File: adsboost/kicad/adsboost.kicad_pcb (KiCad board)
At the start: 4 copper layers, 35.7 x 18 mm, 19 parts, among them J1 ANT_IN, J2 RF_OUT+BIAS, U1 TQP3M9036

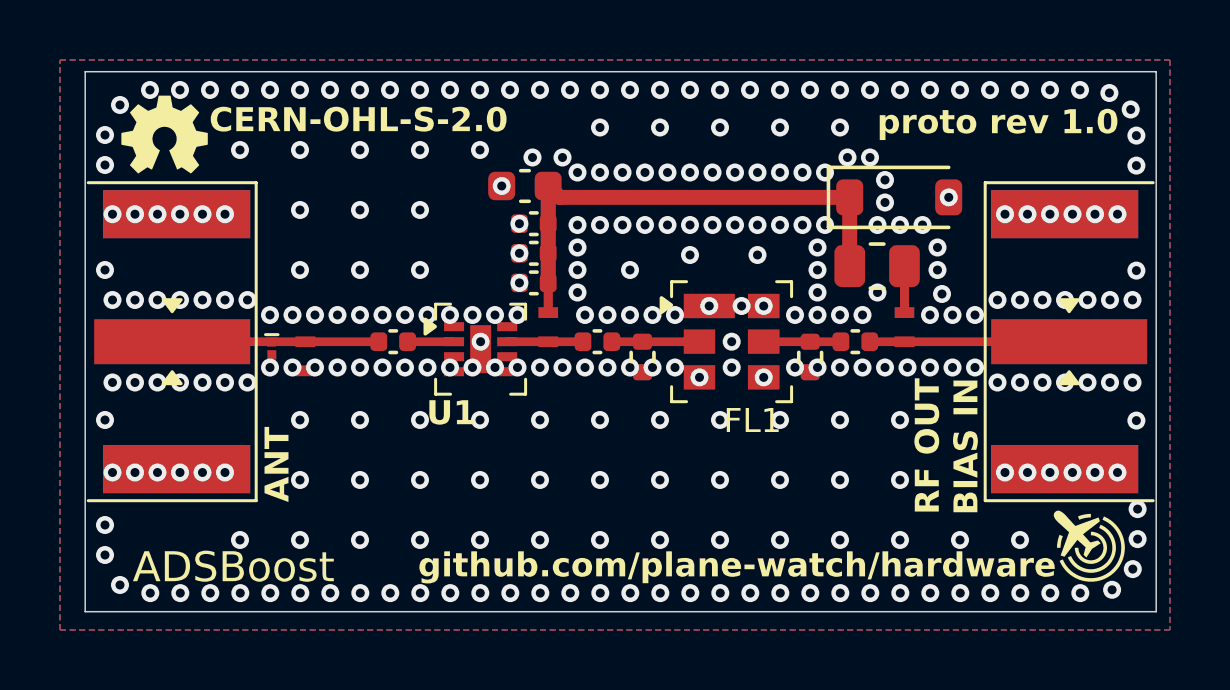
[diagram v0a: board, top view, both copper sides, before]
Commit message: Add RF pi matching networks to ADSBoost
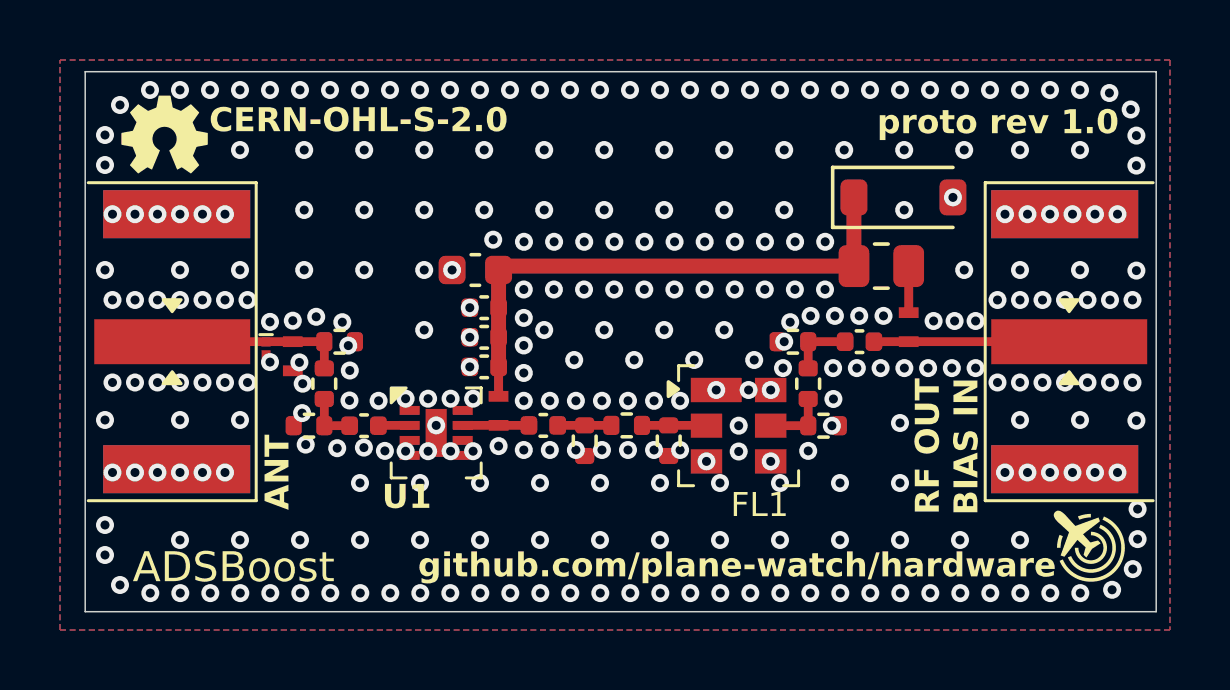
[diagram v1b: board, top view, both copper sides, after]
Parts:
- removed Z1, Z2: RF_SHUNT_DNP, Resistor_SMD:R_0402_1005Metric
- added Z10: 0Ω, Resistor_SMD:R_0402_1005Metric, F.Cu at (150.2, 100.5)
- added Z13: TBD, Resistor_SMD:R_0402_1005Metric, F.Cu at (134.6, 99.1)
- added Z14: TBD, Resistor_SMD:R_0402_1005Metric, F.Cu at (142.7, 102.4)
- added Z15: TBD, Resistor_SMD:R_0402_1005Metric, F.Cu at (133.5, 101.9)
- added Z16: TBD, Resistor_SMD:R_0402_1005Metric, F.Cu at (145.5, 102.4)
- added Z17: TBD, Resistor_SMD:R_0402_1005Metric, F.Cu at (150.7, 101.9)
- added Z18: TBD, Resistor_SMD:R_0402_1005Metric, F.Cu at (149.7, 99.1)
- added Z8: 0Ω, Resistor_SMD:R_0402_1005Metric, F.Cu at (134.1, 100.5)
- added Z9: 0Ω, Resistor_SMD:R_0402_1005Metric, F.Cu at (144.1, 101.9)
- moved C4 3.32 mm to (141.4, 101.9)
- moved C2 3.25 mm to (139.4, 99.9)
- moved C6 3.25 mm to (139.4, 99.0)
- moved C7 3.25 mm to (139.4, 98.0)
- moved C1 3.25 mm to (139.1, 96.7)
- moved L1 3.24 mm to (139.9, 101.4)
- moved U1 3.16 mm to (137.8, 102.1)
- moved C3 2.96 mm to (135.4, 101.9)
- moved FL1 2.81 mm to (147.9, 101.9)
- moved L3 0.42 mm to (133.0, 99.6)
- moved D4 0.19 mm to (132.1, 99.3)
- moved D1 0.14 mm to (153.4, 94.3)
- moved C5 0.14 mm to (151.9, 99.1)
- moved L2 0.14 mm to (153.5, 98.6)
- moved R1 0.14 mm to (152.6, 96.6)
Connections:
- C3 pad 2: Net-(D4-A1) -> Net-(C3-Pad2)
- C4 pad 1: Net-(FL1-IN) -> Net-(C4-Pad1)
- C5 pad 2: Net-(FL1-OUT) -> Net-(C5-Pad2)
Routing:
- net Net-(C5-Pad2): track 0.00 -> 2.12 mm
- net Net-(C4-Pad1): track 0.00 -> 1.79 mm
- net Net-(C3-Pad2): track 0.00 -> 1.73 mm
- net Net-(D1-K): track 16.7 -> 18.4 mm
- net Net-(D4-A1): track 6.89 -> 5.82 mm
- net Net-(FL1-IN): track 2.92 -> 2.15 mm
- net Net-(U1-RF_In): track 1.55 -> 1.04 mm
- net GND: track 0.00 -> 0.01 mm, vias 297 -> 304
